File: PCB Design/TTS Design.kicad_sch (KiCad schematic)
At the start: 21 parts, among them J1 Screw_Terminal_01x02, J2 Screw_Terminal_01x02, J3 Screw_Terminal_01x04, J5 Screw_Terminal_01x03, Q1 IRLZ44N, SW1 SW_DPDT_x2, SW2 SW_DPDT_x2, U1 ESP32-DevKitC, U2 Generic_5v_Module

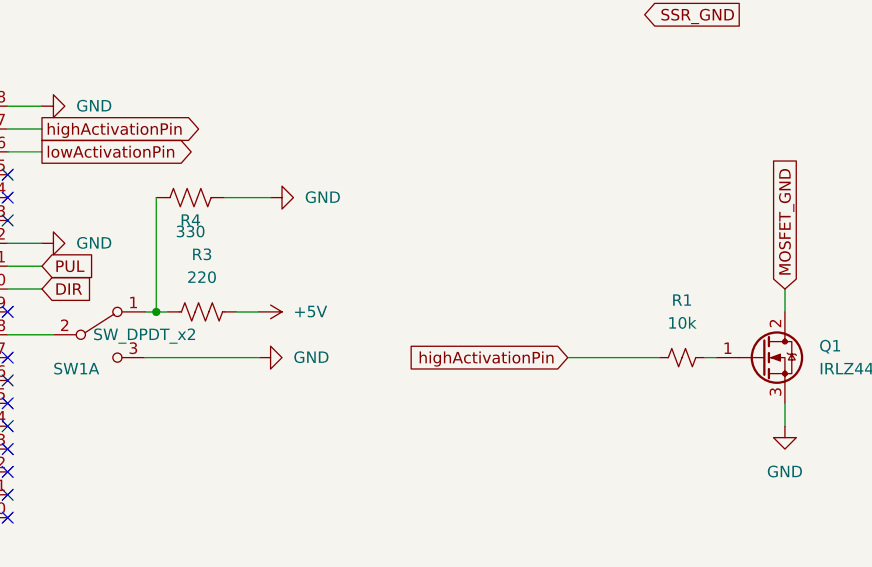
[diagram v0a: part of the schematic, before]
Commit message: Major cleanup of PCB
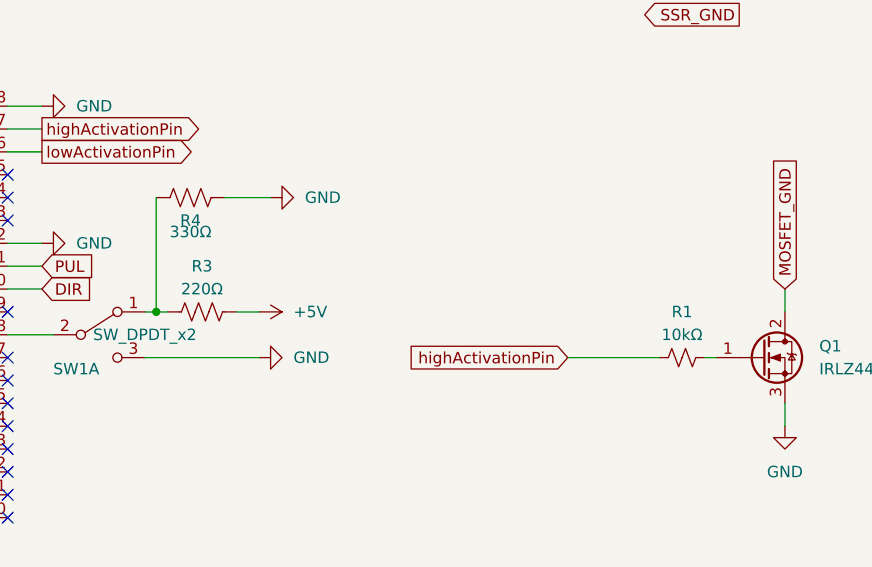
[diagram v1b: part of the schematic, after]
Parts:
- R1: value 10k -> 10kΩ
- R3: value 220 -> 220Ω
- R4: value 330 -> 330Ω
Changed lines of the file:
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@@
     (pin "1")
     (instances
-      (project "DevKitC-4"
+      (project "TTS Design"
         (path "/9dd029d7-3440-476c-a069-461d6098ced3"
           (reference "#PWR0114") (unit 1)
@@
     (pin "1")
     (instances
-      (project "DevKitC-4"
+      (project "TTS Design"
         (path "/9dd029d7-3440-476c-a069-461d6098ced3"
           (reference "#PWR06") (unit 1)
@@
     (pin "3")
     (instances
-      (project "DevKitC-4"
+      (project "TTS Design"
         (path "/9dd029d7-3440-476c-a069-461d6098ced3"
           (reference "RV1") (unit 1)
@@
     (pin "1")
     (instances
-      (project "DevKitC-4"
+      (project "TTS Design"
         (path "/9dd029d7-3440-476c-a069-461d6098ced3"
           (reference "#PWR0105") (unit 1)
@@
     (pin "1")
     (instances
-      (project "DevKitC-4"
+      (project "TTS Design"
         (path "/9dd029d7-3440-476c-a069-461d6098ced3"
           (reference "#PWR0101") (unit 1)
@@
     (pin "6")
     (instances
-      (project "DevKitC-4"
+      (project "TTS Design"
         (path "/9dd029d7-3440-476c-a069-461d6098ced3"
           (reference "SW1") (unit 1)
@@
   (symbol (lib_id "Device:R_US") (at 198.12 121.92 270) (unit 1)
     (in_bom yes) (on_board yes) (dnp no) (fields_autoplaced)
-    (property "Reference" "R3" (at 198.12 115.57 90)
-      (effects (font (size 1.27 1.27)))
-    )
-    (property "Value" "220" (at 198.12 118.11 90)
+    (property "Reference" "R3" (at 198.12 116.84 90)
+      (effects (font (size 1.27 1.27)))
+    )
+    (property "Value" "220Ω" (at 198.12 119.38 90)
       (effects (font (size 1.27 1.27)))
     )
@@
     (pin "2")
     (instances
-      (project "DevKitC-4"
+      (project "TTS Design"
         (path "/9dd029d7-3440-476c-a069-461d6098ced3"
           (reference "R3") (unit 1)
@@
     (pin "1")
     (instances
-      (project "DevKitC-4"
+      (project "TTS Design"
         (path "/9dd029d7-3440-476c-a069-461d6098ced3"
           (reference "#PWR02") (unit 1)
@@
     (pin "1")
     (instances
-      (project "DevKitC-4"
+      (project "TTS Design"
         (path "/9dd029d7-3440-476c-a069-461d6098ced3"
           (reference "#PWR04") (unit 1)
@@
     (pin "1")
     (instances
-      (project "DevKitC-4"
+      (project "TTS Design"
         (path "/9dd029d7-3440-476c-a069-461d6098ced3"
           (reference "#PWR08") (unit 1)
@@
     (pin "1")
     (instances
-      (project "DevKitC-4"
+      (project "TTS Design"
         (path "/9dd029d7-3440-476c-a069-461d6098ced3"
           (reference "#PWR01") (unit 1)
@@
     (pin "1")
     (instances
-      (project "DevKitC-4"
+      (project "TTS Design"
         (path "/9dd029d7-3440-476c-a069-461d6098ced3"
           (reference "#PWR010") (unit 1)
@@
     (pin "2")
     (instances
-      (project "DevKitC-4"
+      (project "TTS Design"
         (path "/9dd029d7-3440-476c-a069-461d6098ced3"
           (reference "C1") (unit 1)
@@
     (pin "1")
     (instances
-      (project "DevKitC-4"
+      (project "TTS Design"
         (path "/9dd029d7-3440-476c-a069-461d6098ced3"
           (reference "#PWR0102") (unit 1)
@@
     (pin "3")
     (instances
-      (project "DevKitC-4"
+      (project "TTS Design"
         (path "/9dd029d7-3440-476c-a069-461d6098ced3"
           (reference "Q1") (unit 1)
@@
     )
     (instances
-      (project "DevKitC-4"
+      (project "TTS Design"
         (path "/9dd029d7-3440-476c-a069-461d6098ced3"
           (reference "H1") (unit 1)
@@
     (pin "1")
     (instances
-      (project "DevKitC-4"
+      (project "TTS Design"
         (path "/9dd029d7-3440-476c-a069-461d6098ced3"
           (reference "#PWR0111") (unit 1)
@@
     (pin "1")
     (instances
-      (project "DevKitC-4"
+      (project "TTS Design"
         (path "/9dd029d7-3440-476c-a069-461d6098ced3"
           (reference "#PWR0113") (unit 1)
@@
     )
     (instances
-      (project "DevKitC-4"
+      (project "TTS Design"
         (path "/9dd029d7-3440-476c-a069-461d6098ced3"
           (reference "H4") (unit 1)
@@
     (pin "3")
     (instances
-      (project "DevKitC-4"
+      (project "TTS Design"
         (path "/9dd029d7-3440-476c-a069-461d6098ced3"
           (reference "J5") (unit 1)
@@
     (pin "1")
     (instances
-      (project "DevKitC-4"
+      (project "TTS Design"
         (path "/9dd029d7-3440-476c-a069-461d6098ced3"
           (reference "#PWR09") (unit 1)
@@
     (pin "1")
     (instances
-      (project "DevKitC-4"
+      (project "TTS Design"
         (path "/9dd029d7-3440-476c-a069-461d6098ced3"
           (reference "#PWR0108") (unit 1)
@@
     )
     (instances
-      (project "DevKitC-4"
+      (project "TTS Design"
         (path "/9dd029d7-3440-476c-a069-461d6098ced3"
           (reference "H3") (unit 1)
@@
     (pin "1")
     (instances
-      (project "DevKitC-4"
+      (project "TTS Design"
         (path "/9dd029d7-3440-476c-a069-461d6098ced3"
           (reference "#PWR0107") (unit 1)
@@
     (pin "1")
     (instances
-      (project "DevKitC-4"
+      (project "TTS Design"
         (path "/9dd029d7-3440-476c-a069-461d6098ced3"
           (reference "#PWR0110") (unit 1)
@@
     (pin "2")
     (instances
-      (project "DevKitC-4"
+      (project "TTS Design"
         (path "/9dd029d7-3440-476c-a069-461d6098ced3"
           (reference "D1") (unit 1)
@@
     (pin "1")
     (instances
-      (project "DevKitC-4"
+      (project "TTS Design"
         (path "/9dd029d7-3440-476c-a069-461d6098ced3"
           (reference "#PWR0104") (unit 1)
@@
     (pin "9")
     (instances
-      (project "DevKitC-4"
+      (project "TTS Design"
         (path "/9dd029d7-3440-476c-a069-461d6098ced3"
           (reference "U1") (unit 1)
@@
     (pin "3")
     (instances
-      (project "DevKitC-4"
+      (project "TTS Design"
         (path "/9dd029d7-3440-476c-a069-461d6098ced3"
           (reference "RV2") (unit 1)
@@
     (pin "6")
     (instances
-      (project "DevKitC-4"
+      (project "TTS Design"
         (path "/9dd029d7-3440-476c-a069-461d6098ced3"
           (reference "SW2") (unit 1)
@@
     (pin "1")
     (instances
-      (project "DevKitC-4"
+      (project "TTS Design"
         (path "/9dd029d7-3440-476c-a069-461d6098ced3"
           (reference "#PWR0103") (unit 1)
@@
     (pin "4")
     (instances
-      (project "DevKitC-4"
+      (project "TTS Design"
         (path "/9dd029d7-3440-476c-a069-461d6098ced3"
           (reference "U2") (unit 1)
@@
     (pin "1")
     (instances
-      (project "DevKitC-4"
+      (project "TTS Design"
         (path "/9dd029d7-3440-476c-a069-461d6098ced3"
           (reference "#PWR07") (unit 1)
@@
     (pin "1")
     (instances
-      (project "DevKitC-4"
+      (project "TTS Design"
         (path "/9dd029d7-3440-476c-a069-461d6098ced3"
           (reference "#PWR03") (unit 1)
@@
     (pin "2")
     (instances
-      (project "DevKitC-4"
+      (project "TTS Design"
         (path "/9dd029d7-3440-476c-a069-461d6098ced3"
           (reference "R6") (unit 1)
@@
     (pin "1")
     (instances
-      (project "DevKitC-4"
+      (project "TTS Design"
         (path "/9dd029d7-3440-476c-a069-461d6098ced3"
           (reference "#PWR0106") (unit 1)
@@
     (pin "2")
     (instances
-      (project "DevKitC-4"
+      (project "TTS Design"
         (path "/9dd029d7-3440-476c-a069-461d6098ced3"
           (reference "J1") (unit 1)
@@
     (pin "4")
     (instances
-      (project "DevKitC-4"
+      (project "TTS Design"
         (path "/9dd029d7-3440-476c-a069-461d6098ced3"
           (reference "J3") (unit 1)
@@
     (pin "1")
     (instances
-      (project "DevKitC-4"
+      (project "TTS Design"
         (path "/9dd029d7-3440-476c-a069-461d6098ced3"
           (reference "#PWR0109") (unit 1)
@@
     )
     (instances
-      (project "DevKitC-4"
+      (project "TTS Design"
         (path "/9dd029d7-3440-476c-a069-461d6098ced3"
           (reference "H2") (unit 1)
@@
     (pin "2")
     (instances
-      (project "DevKitC-4"
+      (project "TTS Design"
         (path "/9dd029d7-3440-476c-a069-461d6098ced3"
           (reference "J2") (unit 1)
@@
   (symbol (lib_id "Device:R_Small_US") (at 251.46 127 90) (unit 1)
     (in_bom yes) (on_board yes) (dnp no) (fields_autoplaced)
-    (property "Reference" "R1" (at 251.46 120.65 90)
-      (effects (font (size 1.27 1.27)))
-    )
-    (property "Value" "10k" (at 251.46 123.19 90)
+    (property "Reference" "R1" (at 251.46 121.92 90)
+      (effects (font (size 1.27 1.27)))
+    )
+    (property "Value" "10kΩ" (at 251.46 124.46 90)
       (effects (font (size 1.27 1.27)))
     )
@@
     (pin "2")
     (instances
-      (project "DevKitC-4"
+      (project "TTS Design"
         (path "/9dd029d7-3440-476c-a069-461d6098ced3"
           (reference "R1") (unit 1)
@@
     (pin "1")
     (instances
-      (project "DevKitC-4"
+      (project "TTS Design"
         (path "/9dd029d7-3440-476c-a069-461d6098ced3"
           (reference "#PWR0112") (unit 1)
@@
       (effects (font (size 1.27 1.27)))
     )
-    (property "Value" "330" (at 196.85 113.03 90)
+    (property "Value" "330Ω" (at 196.85 113.03 90)
       (effects (font (size 1.27 1.27)))
     )
@@
     (pin "2")
     (instances
-      (project "DevKitC-4"
+      (project "TTS Design"
         (path "/9dd029d7-3440-476c-a069-461d6098ced3"
           (reference "R4") (unit 1)

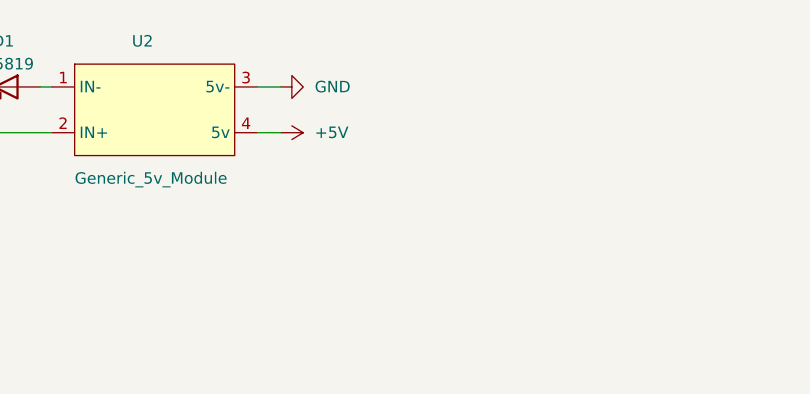
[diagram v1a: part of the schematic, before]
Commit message: PCB change for CAP
Put in 103 cap to smooth out line
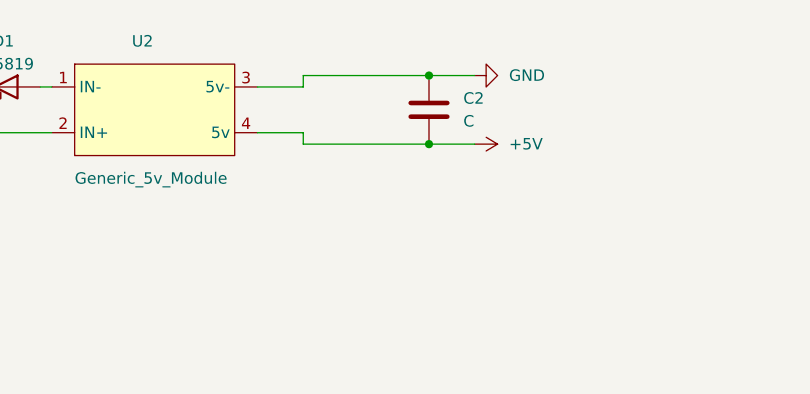
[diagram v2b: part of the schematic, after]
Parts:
- added C2: C, Capacitor_THT:C_Disc_D3.0mm_W1.6mm_P2.50mm, symbol Device:C
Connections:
- net +5V: now also C2.2
- net GND: now also C2.1
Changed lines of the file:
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@@
     (title "ESP32 Turning Target System")
     (date "2022-06-23")
-    (rev "6")
+    (rev "7")
     (company "Scott Dial")
     (comment 1 "Use in conjunction with Bullseye Match from the App Store.")
@@
   (junction (at 193.04 121.92) (diameter 0) (color 0 0 0 0)
   )
+  (junction (at 76.2 19.05) (diameter 0) (color 0 0 0 0)
+  )
   (junction (at 100.33 144.78) (diameter 0) (color 0 0 0 0)
   )
   (junction (at 100.33 132.08) (diameter 0) (color 0 0 0 0)
+  )
+  (junction (at 76.2 26.67) (diameter 0) (color 0 0 0 0)
   )
   (no_connect (at 106.68 129.54))
@@
     (stroke (width 0) (type default))
   )
+  (wire (pts (xy 76.2 19.05) (xy 81.28 19.05))
+    (stroke (width 0) (type default))
+  )
   (wire (pts (xy 176.53 101.6) (xy 180.34 101.6))
     (stroke (width 0) (type default))
   )
-  (wire (pts (xy 57.15 20.32) (xy 59.69 20.32))
-    (stroke (width 0) (type default))
-  )
   (wire (pts (xy 74.93 121.92) (xy 62.23 121.92))
     (stroke (width 0) (type default))
@@
     (stroke (width 0) (type default))
   )
+  (wire (pts (xy 62.23 19.05) (xy 76.2 19.05))
+    (stroke (width 0) (type default))
+  )
   (wire (pts (xy 99.06 132.08) (xy 100.33 132.08))
     (stroke (width 0) (type default))
@@
     (stroke (width 0) (type default))
   )
+  (wire (pts (xy 76.2 26.67) (xy 62.23 26.67))
+    (stroke (width 0) (type default))
+  )
   (wire (pts (xy 262.89 76.2) (xy 262.89 77.47))
     (stroke (width 0) (type default))
@@
     (stroke (width 0) (type default))
   )
+  (wire (pts (xy 76.2 26.67) (xy 81.28 26.67))
+    (stroke (width 0) (type default))
+  )
   (wire (pts (xy 140.97 64.77) (xy 144.78 64.77))
     (stroke (width 0) (type default))
@@
     (stroke (width 0) (type default))
   )
+  (wire (pts (xy 62.23 25.4) (xy 57.15 25.4))
+    (stroke (width 0) (type default))
+  )
   (wire (pts (xy 140.97 69.85) (xy 144.78 69.85))
     (stroke (width 0) (type default))
@@
     (stroke (width 0) (type default))
   )
-  (wire (pts (xy 57.15 25.4) (xy 59.69 25.4))
-    (stroke (width 0) (type default))
-  )
   (wire (pts (xy 262.89 132.08) (xy 262.89 134.62))
     (stroke (width 0) (type default))
@@
     (stroke (width 0) (type default))
   )
+  (wire (pts (xy 57.15 20.32) (xy 62.23 20.32))
+    (stroke (width 0) (type default))
+  )
   (wire (pts (xy 193.04 109.22) (xy 193.04 121.92))
     (stroke (width 0) (type default))
   )
+  (wire (pts (xy 62.23 20.32) (xy 62.23 19.05))
+    (stroke (width 0) (type default))
+  )
   (wire (pts (xy 104.14 99.06) (xy 106.68 99.06))
     (stroke (width 0) (type default))
   )
   (wire (pts (xy 104.14 109.22) (xy 106.68 109.22))
+    (stroke (width 0) (type default))
+  )
+  (wire (pts (xy 62.23 26.67) (xy 62.23 25.4))
     (stroke (width 0) (type default))
   )
@@
     )
   )
+  (symbol (lib_id "Device:C") (at 76.2 22.86 0) (unit 1)
+    (in_bom yes) (on_board yes) (dnp no) (fields_autoplaced)
+    (property "Reference" "C2" (at 80.01 21.59 0)
+      (effects (font (size 1.27 1.27)) (justify left))
+    )
+    (property "Value" "C" (at 80.01 24.13 0)
+      (effects (font (size 1.27 1.27)) (justify left))
+    )
+    (property "Footprint" "Capacitor_THT:C_Disc_D3.0mm_W1.6mm_P2.50mm" (at 77.1652 26.67 0)
+      (effects (font (size 1.27 1.27)) hide)
+    )
+    (property "Datasheet" "~" (at 76.2 22.86 0)
+      (effects (font (size 1.27 1.27)) hide)
+    )
+    (pin "1")
+    (pin "2")
+    (instances
+      (project "TTS Design"
+        (path "/9dd029d7-3440-476c-a069-461d6098ced3"
+          (reference "C2") (unit 1)
+        )
+      )
+    )
+  )
+  (symbol (lib_name "GND_1") (lib_id "power:GND") (at 81.28 19.05 90) (unit 1)
+    (in_bom yes) (on_board yes) (dnp no) (fields_autoplaced)
+    (property "Reference" "#PWR05" (at 87.63 19.05 0)
+      (effects (font (size 1.27 1.27)) hide)
+    )
+    (property "Value" "GND" (at 85.09 19.05 90)
+      (effects (font (size 1.27 1.27)) (justify right))
+    )
+    (property "Footprint" "" (at 81.28 19.05 0)
+      (effects (font (size 1.27 1.27)) hide)
+    )
+    (property "Datasheet" "" (at 81.28 19.05 0)
+      (effects (font (size 1.27 1.27)) hide)
+    )
+    (pin "1")
+    (instances
+      (project "TTS Design"
+        (path "/9dd029d7-3440-476c-a069-461d6098ced3"
+          (reference "#PWR05") (unit 1)
+        )
+      )
+    )
+  )
   (symbol (lib_id "power:GND") (at 262.89 134.62 0) (unit 1)
     (in_bom yes) (on_board yes) (dnp no) (fields_autoplaced)
@@
         (path "/9dd029d7-3440-476c-a069-461d6098ced3"
           (reference "#PWR04") (unit 1)
-        )
-      )
-    )
-  )
-  (symbol (lib_id "power:GND") (at 59.69 20.32 90) (unit 1)
-    (in_bom yes) (on_board yes) (dnp no) (fields_autoplaced)
-    (property "Reference" "#PWR08" (at 66.04 20.32 0)
-      (effects (font (size 1.27 1.27)) hide)
-    )
-    (property "Value" "GND" (at 63.5 20.3199 90)
-      (effects (font (size 1.27 1.27)) (justify right))
-    )
-    (property "Footprint" "" (at 59.69 20.32 0)
-      (effects (font (size 1.27 1.27)) hide)
-    )
-    (property "Datasheet" "" (at 59.69 20.32 0)
-      (effects (font (size 1.27 1.27)) hide)
-    )
-    (pin "1")
-    (instances
-      (project "TTS Design"
-        (path "/9dd029d7-3440-476c-a069-461d6098ced3"
-          (reference "#PWR08") (unit 1)
         )
       )
@@
     )
   )
-  (symbol (lib_id "power:+5V") (at 59.69 25.4 270) (unit 1)
-    (in_bom yes) (on_board yes) (dnp no) (fields_autoplaced)
-    (property "Reference" "#PWR07" (at 55.88 25.4 0)
-      (effects (font (size 1.27 1.27)) hide)
-    )
-    (property "Value" "+5V" (at 63.5 25.3999 90)
-      (effects (font (size 1.27 1.27)) (justify left))
-    )
-    (property "Footprint" "" (at 59.69 25.4 0)
-      (effects (font (size 1.27 1.27)) hide)
-    )
-    (property "Datasheet" "" (at 59.69 25.4 0)
-      (effects (font (size 1.27 1.27)) hide)
-    )
+  (symbol (lib_id "power:+5V") (at 81.28 26.67 270) (unit 1)
+    (in_bom yes) (on_board yes) (dnp no) (fields_autoplaced)
+    (property "Reference" "#PWR07" (at 77.47 26.67 0)
+      (effects (font (size 1.27 1.27)) hide)
+    )
+    (property "Value" "+5V" (at 85.09 26.6699 90)
+      (effects (font (size 1.27 1.27)) (justify left))
+    )
+    (property "Footprint" "" (at 81.28 26.67 0)
+      (effects (font (size 1.27 1.27)) hide)
+    )
+    (property "Datasheet" "" (at 81.28 26.67 0)
+      (effects (font (size 1.27 1.27)) hide)
+    )

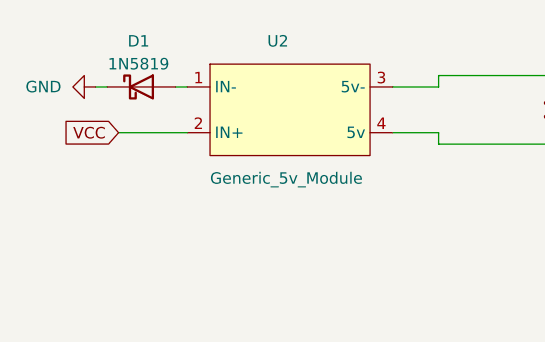
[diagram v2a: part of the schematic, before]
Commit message: PCB changes for Diode
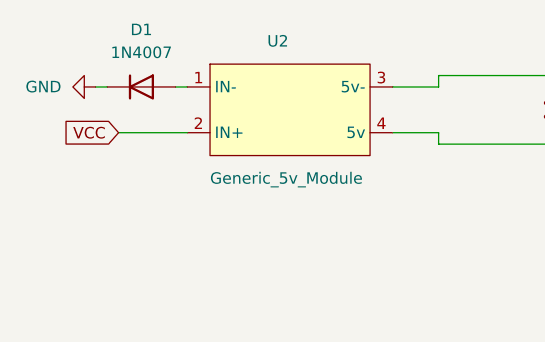
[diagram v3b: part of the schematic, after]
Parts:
- D1: value 1N5819 -> 1N4007; symbol Diode:1N5819 -> Diode:1N4007
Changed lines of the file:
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@@
     )
   )
-  (symbol (lib_id "Diode:1N5819") (at 29.21 20.32 0) (unit 1)
+  (symbol (lib_id "Diode:1N4007") (at 29.21 20.32 0) (unit 1)
     (in_bom yes) (on_board yes) (dnp no) (fields_autoplaced)
-    (property "Reference" "D1" (at 28.8925 15.24 0)
+    (property "Reference" "D1" (at 29.21 13.97 0)
       (effects (font (size 1.27 1.27)))
     )
-    (property "Value" "1N5819" (at 28.8925 17.78 0)
+    (property "Value" "1N4007" (at 29.21 16.51 0)
       (effects (font (size 1.27 1.27)))
     )
@@
       (effects (font (size 1.27 1.27)) hide)
     )
-    (property "Datasheet" "http://www.vishay.com/docs/88525/1n5817.pdf" (at 29.21 20.32 0)
+    (property "Datasheet" "http://www.vishay.com/docs/88503/1n4001.pdf" (at 29.21 20.32 0)
       (effects (font (size 1.27 1.27)) hide)
     )
+    (property "Sim.Device" "D" (at 29.21 20.32 0)
+      (effects (font (size 1.27 1.27)) hide)
+    )
+    (property "Sim.Pins" "1=K 2=A" (at 29.21 20.32 0)
+      (effects (font (size 1.27 1.27)) hide)
+    )
